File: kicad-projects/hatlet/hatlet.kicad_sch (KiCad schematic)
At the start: 49 parts, among them J2 SWD, J3 PMOD0, J4 PMOD2, J5 PMOD1, J6 UART0, J7 PMOD3, J8 USB Header, SW1 BOOTSEL, U1 AMS1117-3.3, U2 RP2040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

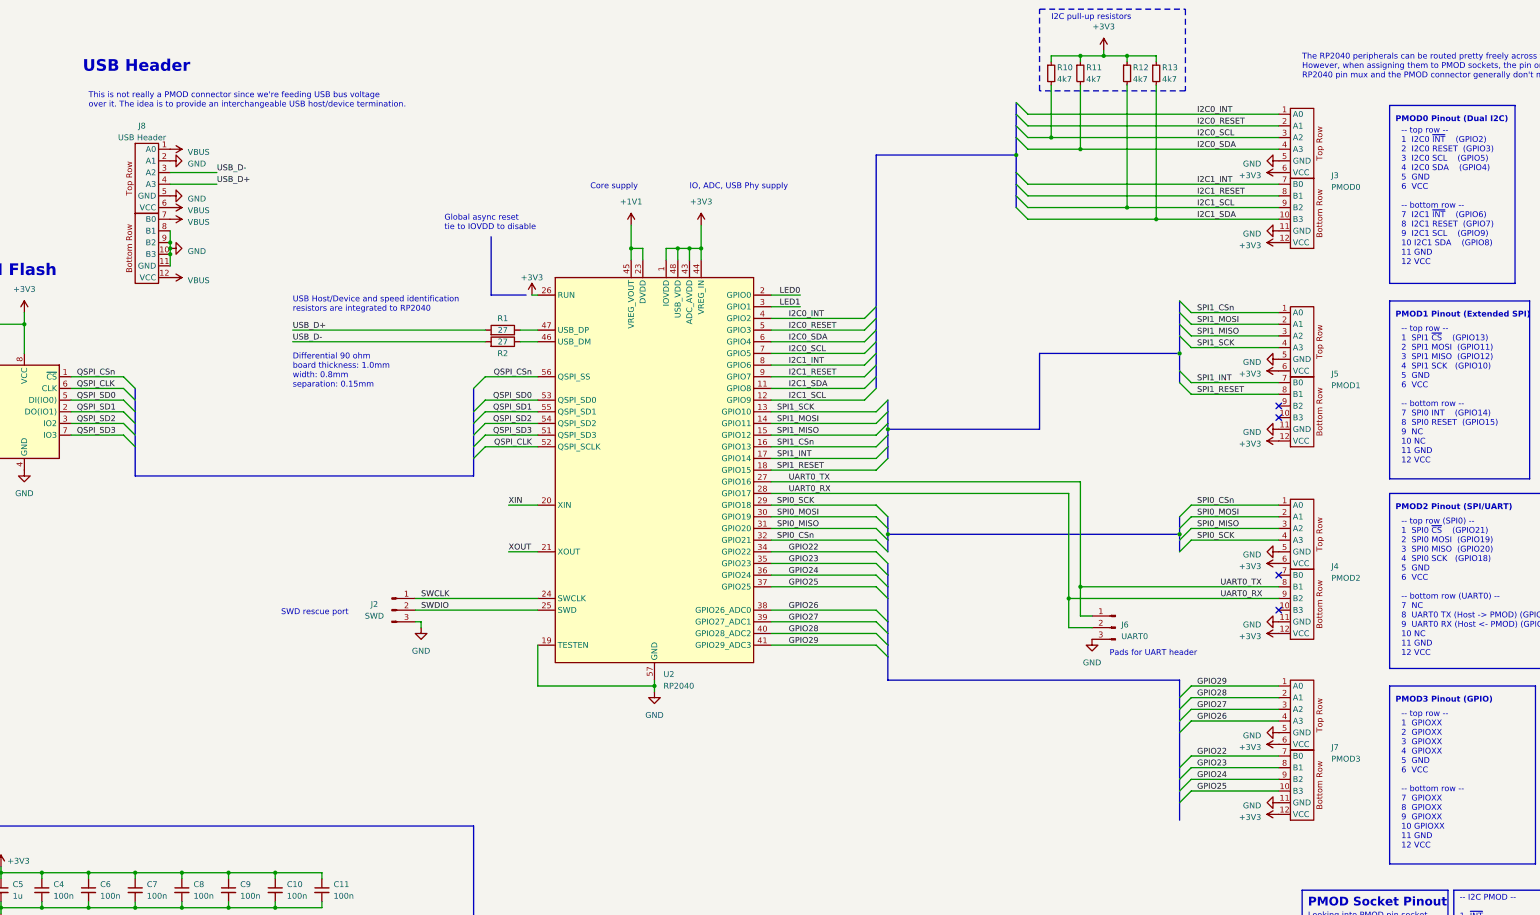
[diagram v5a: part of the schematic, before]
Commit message: Use USB header from racklet-kicad-lib
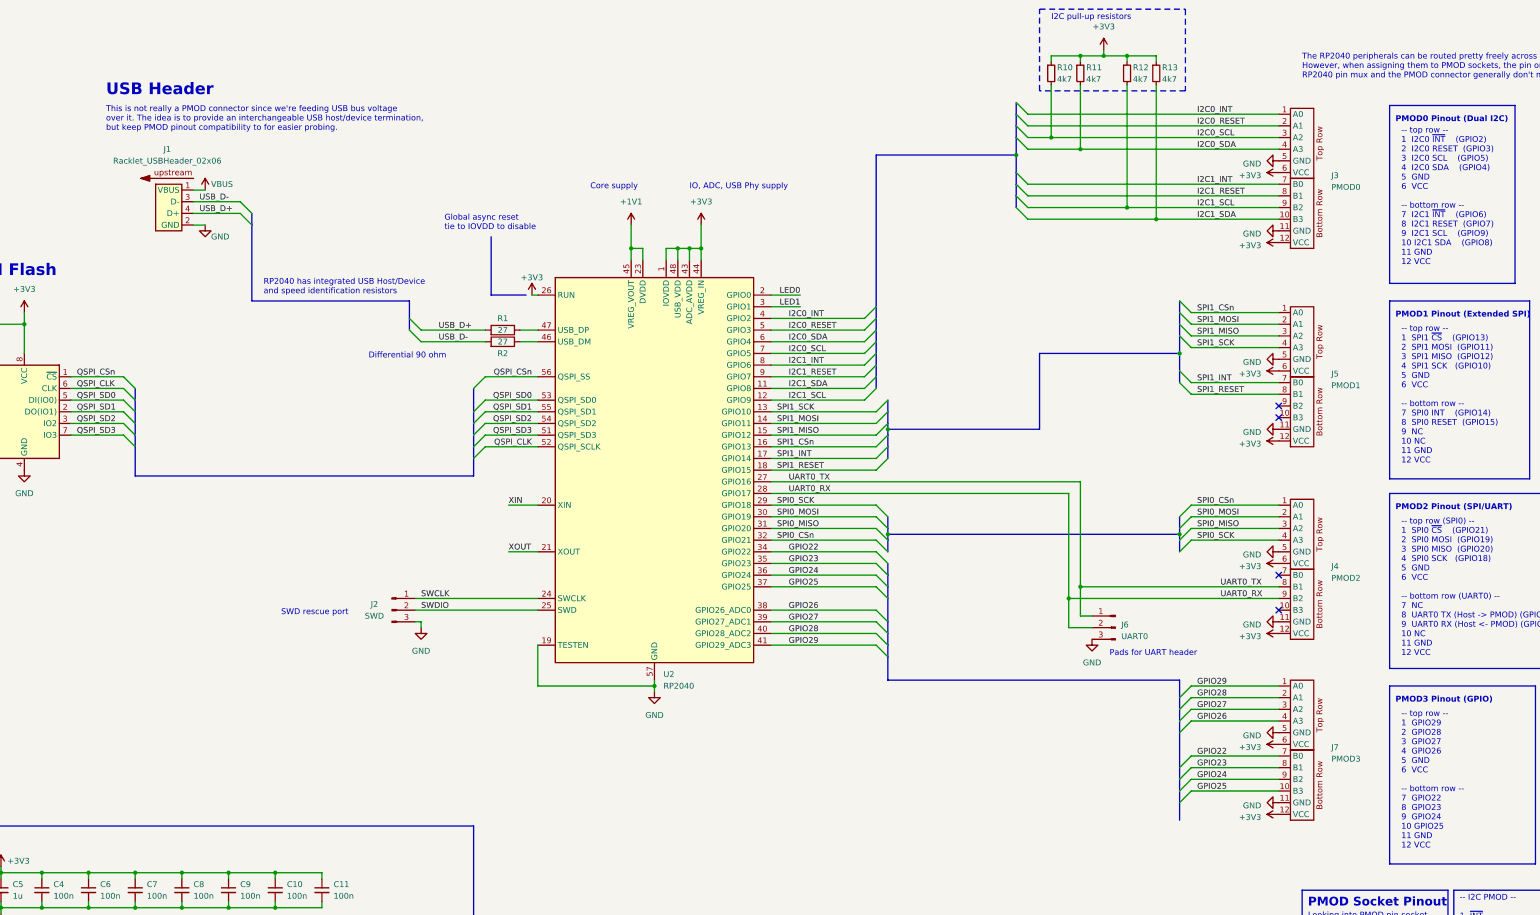
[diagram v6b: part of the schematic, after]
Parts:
- removed J8: USB Header, racklet:Racklet_USBHeader_02x06, symbol pmod:PMOD_Peripheral_Conn_02x06
- added J1: Racklet_USBHeader_02x06, racklet:Racklet_USBHeader_02x06, symbol racklet:Racklet_USBHeader_02x06
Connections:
- net GND: now also J1.11 (GND), J1.2 (GND), J1.5 (GND), J1.8 (GND)
- net USB_D+: now also J1.4 (D+), J1.9 (D+)
- net USB_D-: now also J1.10 (D-), J1.3 (D-)
- net VBUS: now also J1.1 (VBUS), J1.12 (VBUS), J1.6 (VBUS), J1.7 (VBUS)
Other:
- note added: "-- top row -- 1 GPIO29 2 GPIO28 3 GPIO27 4 GPIO26 5 GND 6 VCC -- bottom row -- 7 GPIO22 8 GPIO23 9 GPIO24 10 GPIO25 11 GND 12 VCC"
- note added: "Differential 90 ohm"
- note added: "RP2040 has integrated USB Host/Device and speed identification resistors"
- note added: "This is not really a PMOD connector since we're feeding USB bus voltage over it. The idea is to provide an interchangeable USB host/device termination, but keep PMOD pinout compatibility to for easier probing."
- note removed: "-- top row -- 1 GPIOXX 2 GPIOXX 3 GPIOXX 4 GPIOXX 5 GND 6 VCC -- bottom row -- 7 GPIOXX 8 GPIOXX 9 GPIOXX 10 GPIOXX 11 GND 12 VCC"
- note removed: "Differential 90 ohm board thickness: 1.0mm width: 0.8mm separation: 0.15mm"
- note removed: "This is not really a PMOD connector since we're feeding USB bus voltage over it. The idea is to provide an interchangeable USB host/device termination."
- note removed: "USB Host/Device and speed identification resistors are integrated to RP2040"

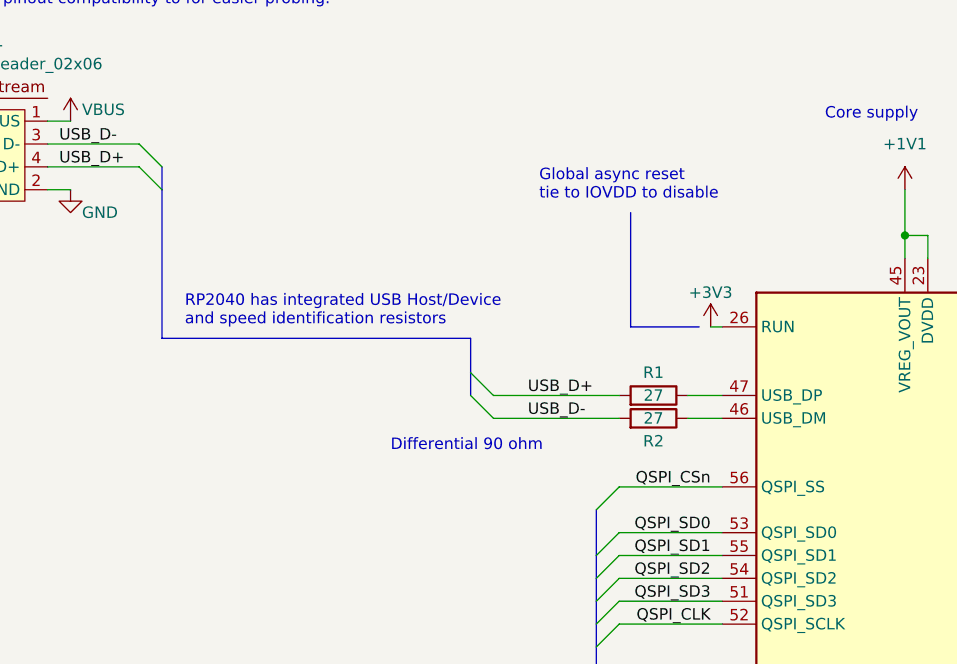
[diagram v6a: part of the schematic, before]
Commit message: hatlet: add reset button
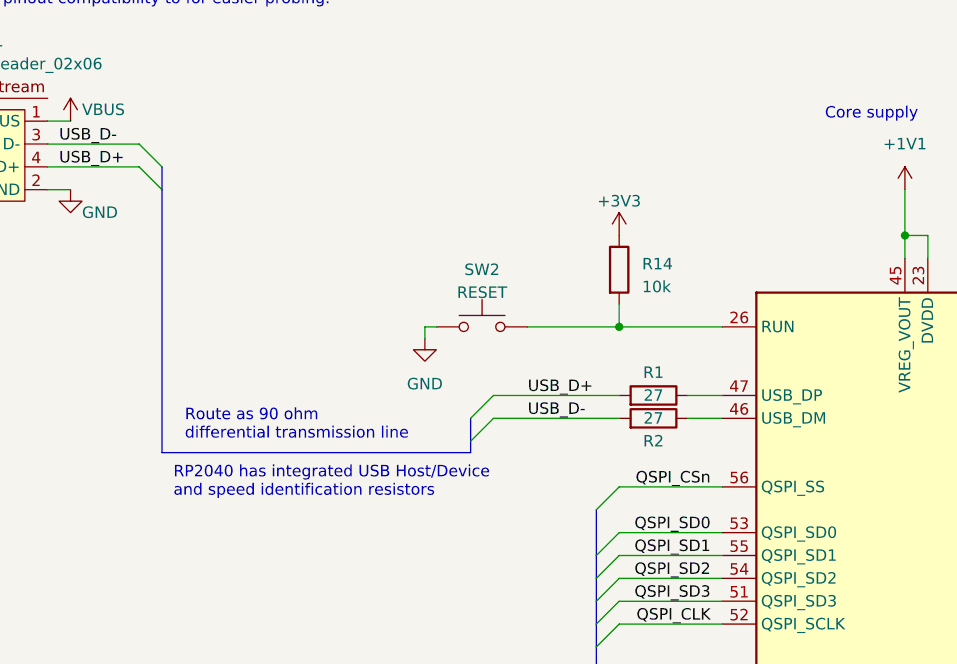
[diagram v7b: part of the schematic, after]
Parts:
- added R14: 10k, Resistor_SMD:R_0603_1608Metric, symbol Device:R
- added SW2: RESET, Button_Switch_SMD:SW_SPST_TL3342, symbol Switch:SW_Push
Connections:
- net +3V3: now also R14.1; no longer U2.26 (RUN)
- net GND: now also SW2.1
- new net: R14.2, SW2.2, U2.26 (RUN)
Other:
- note added: "Route as 90 ohm differential transmission line"
- note removed: "Differential 90 ohm"
- note removed: "Global async reset tie to IOVDD to disable"
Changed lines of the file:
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@@
     (comment 1 "Authors: Verneri Hirvonen (2023)")
+  )
+  (junction (at 149.86 76.2) (diameter 0) (color 0 0 0 0)
   )
   (junction (at 83.82 201.93) (diameter 0) (color 0 0 0 0)
@@
     (stroke (width 0) (type default))
   )
-  (bus_entry (at 133.35 83.82) (size 2.54 2.54)
+  (bus_entry (at 133.35 88.9) (size 2.54 -2.54)
     (stroke (width 0) (type default))
   )
@@
     (stroke (width 0) (type default))
   )
-  (bus_entry (at 133.35 81.28) (size 2.54 2.54)
+  (bus_entry (at 133.35 86.36) (size 2.54 -2.54)
     (stroke (width 0) (type default))
   )
@@
     (stroke (width 0) (type default))
   )
-  (bus (pts (xy 133.35 83.82) (xy 133.35 81.28))
+  (wire (pts (xy 149.86 76.2) (xy 149.86 73.66))
+    (stroke (width 0) (type default))
+  )
+  (wire (pts (xy 161.29 76.2) (xy 149.86 76.2))
     (stroke (width 0) (type default))
   )
@@
     (stroke (width 0) (type default))
   )
+  (wire (pts (xy 128.27 77.47) (xy 128.27 76.2))
+    (stroke (width 0) (type default))
+  )
   (wire (pts (xy 289.56 24.13) (xy 289.56 25.4))
     (stroke (width 0) (type default))
@@
     (stroke (width 0) (type default))
   )
-  (bus (pts (xy 99.06 60.96) (xy 99.06 77.47))
+  (bus (pts (xy 99.06 60.96) (xy 99.06 90.17))
     (stroke (width 0) (type default))
   )
@@
     (stroke (width 0) (type default))
   )
+  (bus (pts (xy 133.35 88.9) (xy 133.35 90.17))
+    (stroke (width 0) (type default))
+  )
   (wire (pts (xy 149.86 86.36) (xy 135.89 86.36))
     (stroke (width 0) (type default))
@@
     (stroke (width 0) (type default))
   )
-  (polyline (pts (xy 151.13 63.5) (xy 151.13 76.2))
-    (stroke (width 0) (type default))
-  )
   (wire (pts (xy 53.34 226.06) (xy 53.34 227.33))
     (stroke (width 0) (type default))
@@
     (stroke (width 0) (type default))
   )
-  (polyline (pts (xy 158.75 76.2) (xy 151.13 76.2))
-    (stroke (width 0) (type default))
-  )
   (bus (pts (xy 237.49 149.86) (xy 237.49 152.4))
     (stroke (width 0) (type default))
   )
+  (bus (pts (xy 133.35 86.36) (xy 133.35 88.9))
+    (stroke (width 0) (type default))
+  )
   (bus (pts (xy 237.49 124.46) (xy 237.49 127))
     (stroke (width 0) (type default))
@@
     (stroke (width 0) (type default))
   )
+  (wire (pts (xy 139.7 76.2) (xy 149.86 76.2))
+    (stroke (width 0) (type default))
+  )
   (wire (pts (xy 186.69 162.56) (xy 186.69 161.29))
     (stroke (width 0) (type default))
@@
     (stroke (width 0) (type default))
   )
-  (bus (pts (xy 133.35 81.28) (xy 133.35 77.47))
-    (stroke (width 0) (type default))
-  )
   (wire (pts (xy 322.58 121.92) (xy 303.53 121.92))
     (stroke (width 0) (type default))
@@
     (stroke (width 0) (type default))
   )
-  (wire (pts (xy 160.02 76.2) (xy 161.29 76.2))
-    (stroke (width 0) (type default))
-  )
   (bus (pts (xy 237.49 129.54) (xy 237.49 132.08))
     (stroke (width 0) (type default))
@@
     (stroke (width 0) (type default))
   )
-  (bus (pts (xy 133.35 77.47) (xy 99.06 77.47))
+  (bus (pts (xy 133.35 90.17) (xy 99.06 90.17))
     (stroke (width 0) (type default))
   )
@@
   )
   (wire (pts (xy 212.09 152.4) (xy 234.95 152.4))
+    (stroke (width 0) (type default))
+  )
+  (wire (pts (xy 128.27 76.2) (xy 129.54 76.2))
     (stroke (width 0) (type default))
   )
@@
     (effects (font (size 1.27 1.27) (thickness 0.254) bold) (justify left bottom))
   )
-  (text "Differential 90 ohm" (at 124.46 90.17 0)
+  (text "Route as 90 ohm\ndifferential transmission line" (at 101.6 88.9 0)
     (effects (font (size 1.27 1.27)) (justify left bottom))
   )
@@
   )
   (text "RP2040 has integrated USB Host/Device\nand speed identification resistors"
-    (at 101.6 76.2 0)
+    (at 100.33 95.25 0)
     (effects (font (size 1.27 1.27)) (justify left bottom))
   )
@@
   (text "3" (at 345.44 217.805 0)
     (effects (font (size 1.27 1.27) bold) (justify right bottom))
-  )
-  (text "Global async reset\ntie to IOVDD to disable" (at 140.97 62.23 0)
-    (effects (font (size 1.27 1.27)) (justify left bottom))
   )
   (text "Core supply" (at 172.72 53.34 0)
@@
     )
   )
-  (symbol (lib_id "power:+3V3") (at 160.02 76.2 0) (unit 1)
+  (symbol (lib_id "power:+3V3") (at 149.86 66.04 0) (unit 1)
     (in_bom yes) (on_board yes) (dnp no) (fields_autoplaced)
-    (property "Reference" "#PWR026" (at 160.02 80.01 0)
-      (effects (font (size 1.27 1.27)) hide)
-    )
-    (property "Value" "+3V3" (at 160.02 72.39 0)
+    (property "Reference" "#PWR026" (at 149.86 69.85 0)
+      (effects (font (size 1.27 1.27)) hide)
+    )
+    (property "Value" "+3V3" (at 149.86 62.23 0)
       (effects (font (size 1.27 1.27)))
     )
-    (property "Footprint" "" (at 160.02 76.2 0)
-      (effects (font (size 1.27 1.27)) hide)
-    )
-    (property "Datasheet" "" (at 160.02 76.2 0)
+    (property "Footprint" "" (at 149.86 66.04 0)
+      (effects (font (size 1.27 1.27)) hide)
+    )
+    (property "Datasheet" "" (at 149.86 66.04 0)
       (effects (font (size 1.27 1.27)) hide)
     )
@@
     )
   )
+  (symbol (lib_id "Device:R") (at 149.86 69.85 0) (unit 1)
+    (in_bom yes) (on_board yes) (dnp no)
+    (property "Reference" "R14" (at 152.4 69.215 0)
+      (effects (font (size 1.27 1.27)) (justify left))
+    )
+    (property "Value" "10k" (at 152.4 71.755 0)
+      (effects (font (size 1.27 1.27)) (justify left))
+    )
+    (property "Footprint" "Resistor_SMD:R_0603_1608Metric" (at 148.082 69.85 90)
+      (effects (font (size 1.27 1.27)) hide)
+    )
+    (property "Datasheet" "~" (at 149.86 69.85 0)
+      (effects (font (size 1.27 1.27)) hide)
+    )
+    (property "JLCPCB Part #" "C25804" (at 149.86 69.85 0)
+      (effects (font (size 1.27 1.27)) hide)
+    )
+    (pin "1")
+    (pin "2")
+    (instances
+      (project "hatlet"
+        (path "/422c1aa7-bd8c-4c94-9e5b-2fd049d9e649"
+          (reference "R14") (unit 1)
+        )
+      )
+    )
+  )
   (symbol (lib_name "GND_5") (lib_id "power:GND") (at 270.51 273.05 0) (unit 1)
     (in_bom yes) (on_board yes) (dnp no) (fields_autoplaced)
@@
         (path "/422c1aa7-bd8c-4c94-9e5b-2fd049d9e649"
           (reference "R5") (unit 1)
+        )
+      )
+    )
+  )
+  (symbol (lib_name "GND_13") (lib_id "power:GND") (at 128.27 77.47 0) (unit 1)
+    (in_bom yes) (on_board yes) (dnp no) (fields_autoplaced)
+    (property "Reference" "#PWR06" (at 128.27 83.82 0)
+      (effects (font (size 1.27 1.27)) hide)
+    )
+    (property "Value" "GND" (at 128.27 82.55 0)
+      (effects (font (size 1.27 1.27)))
+    )
+    (property "Footprint" "" (at 128.27 77.47 0)
+      (effects (font (size 1.27 1.27)) hide)
+    )
+    (property "Datasheet" "" (at 128.27 77.47 0)
+      (effects (font (size 1.27 1.27)) hide)
+    )
+    (pin "1")
+    (instances
+      (project "hatlet"
+        (path "/422c1aa7-bd8c-4c94-9e5b-2fd049d9e649"
+          (reference "#PWR06") (unit 1)
         )
       )
@@
         )
       )
+    )
+  )
+  (symbol (lib_id "Switch:SW_Push") (at 134.62 76.2 0) (unit 1)
+    (in_bom yes) (on_board yes) (dnp no) (fields_autoplaced)
+    (property "Reference" "SW2" (at 134.62 69.85 0)
+      (effects (font (size 1.27 1.27)))
+    )
+    (property "Value" "RESET" (at 134.62 72.39 0)
+      (effects (font (size 1.27 1.27)))
+    )
+    (property "Footprint" "Button_Switch_SMD:SW_SPST_TL3342" (at 134.62 71.12 0)
+      (effects (font (size 1.27 1.27)) hide)
+    )
+    (property "Datasheet" "https://datasheet.lcsc.com/lcsc/2104141846_G-Switch-GT-TC084C-H015-L5_C2762971.pdf" (at 134.62 71.12 0)
+      (effects (font (size 1.27 1.27)) hide)
+    )
+    (property "JLCPCB Part #" "C318884" (at 134.62 76.2 0)
+      (effects (font (size 1.27 1.27)) hide)
+    )
+    (pin "1")
+    (pin "2")
+    (instances
+      (project "hatlet"
+        (path "/422c1aa7-bd8c-4c94-9e5b-2fd049d9e649"
+          (reference "SW2") (unit 1)
+        )
+      )
